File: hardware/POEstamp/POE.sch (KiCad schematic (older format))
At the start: 56 parts, among them J1 0813-1X1T-57-F, P1 PoE-, P2 PoE+, P3 GND, P4 +5V, Q1 SI3440DV, NFET, Q2 MMBTA42, Q3 2N7002, T1 PA1134, U1 LTC4267-3, U3 PS2811

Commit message: Finished adding BOM info to schematic. Swapped around a couple more symbols and footprints. Ran DRC and corrected one error.
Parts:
- removed Q2: MMBTA42, SMD_Packages:SOT-23_Inv2, symbol NPN
- removed Q3: 2N7002, SMD_Packages:SOT-23-GDS, symbol MOSFET_N
- removed R21: 470R, IPC7351-Nominal:RESC1608X55, symbol R-RESCUE-POE
- added P5: CONN_01X05, symbol CONN_01X05
- added P6: 5Vout, symbol TST
- added P7: GNDout, symbol TST
- added Q2: 2N7002, smd-semi:SOT-23, symbol MMBF170
- added Q3: MMBTA42, smd-semi:SOT-23, symbol MMBT3904
- added R21: 470R, IPC7351-Nominal:RESC1608X55, symbol R
- J1: Vend1 (none) -> Digikey; Vend1Id (none) -> 507-1421-ND
- Q1: footprint (none) -> rfid:TSOP-6; Vend1 (none) -> Digikey; Vend1Id (none) -> SI3440DV-T1-E3CT-ND
- T1: Vend1 (none) -> Digikey; Vend1Id (none) -> 553-1982-1-ND
- U3: Vend1 (none) -> Digikey; Vend1Id (none) -> PS2811-1ACT-ND
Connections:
- net 5VPoE: now also P6.1, R21.1
- net GND: now also P7.1
- net GNDA: now also Q2.2 (S)
- net Ith/Run: now also Q2.3 (D)
- net PVcc: now also Q3.2 (E)
- net TPIN+: now also P5.3 (P3)
- net TPIN-: now also P5.4 (P4)
- net TPOUT+: now also P5.1 (P1)
- net TPOUT-: now also P5.2 (P2)
- net at C2.1, C3.1, L1.2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: now also Q3.3 (C)
- net at D5.2 (K), R2.2: now also Q3.1 (B)
- net at D4.2 (K), R1.2: now also Q2.1 (G)
- net at C12.1, C13.1, R11.1: now also R21.2
- net CT: now reaches J1.7 (CT)
- net CT: now also P5.5 (P5)
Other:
- note added: "Power out"
- note added: "power good\nvisual indicator"
- note removed: "power good visual indicator"
- moved on the sheet: D12, R22
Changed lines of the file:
@@
-$EndComp
-$Comp
-L NPN Q2
-U 1 1 52997F92
-P 7450 3205
-F 0 "Q2" H 7450 3055 50  0000 R CNN
-F 1 "MMBTA42" H 7450 3355 50  0000 R CNN
-F 2 "SMD_Packages:SOT-23_Inv2" H 7450 3205 60  0001 C CNN
-F 3 "" H 7450 3205 60  0000 C CNN
-	1    7450 3205
-	1    0    0    -1
 $EndComp
 $Comp
@@
 F 1 "PA1134" H 9815 3425 50  0000 C CNN
 F 2 "rfid:PA1134" V 9850 2865 60  0001 C CNN
-F 3 "" V 9850 2865 60  0000 C CNN
+F 3 "http://productfinder.pulseeng.com/products/datasheets/SPM2007_55.pdf" V 9850 2865 60  0001 C CNN
+F 4 "Digikey" H 9750 3015 60  0001 C CNN "Vend1"
+F 5 "553-1982-1-ND" H 9750 3015 60  0001 C CNN "Vend1Id"
 	1    9750 3015
 	1    0    0    -1
@@
 NoConn ~ 4450 4465
 $Comp
-L MOSFET_N Q3
-U 1 1 529FE736
-P 7300 4865
-F 0 "Q3" V 7150 5065 60  0000 R CNN
-F 1 "2N7002" V 7500 5015 60  0000 R CNN
-F 2 "SMD_Packages:SOT-23-GDS" H 7300 4865 60  0001 C CNN
-F 3 "" H 7300 4865 60  0000 C CNN
-	1    7300 4865
-	0    1    1    0
-$EndComp
-$Comp
 L DIODE-RESCUE-POE D7
 U 1 1 529FE790
@@
 F 1 "PS2811" H 10435 5940 70  0000 C CNN
 F 2 "rfid:SSOP-4" H 9995 5565 60  0001 C CNN
-F 3 "" H 9995 5565 60  0000 C CNN
+F 3 "http://www.cel.com/pdf/datasheets/ps2811.pdf" H 9995 5565 60  0001 C CNN
+F 4 "Digikey" H 9395 5565 60  0001 C CNN "Vend1"
+F 5 "PS2811-1ACT-ND" H 9395 5565 60  0001 C CNN "Vend1Id"
 	1    9395 5565
 	1    0    0    -1
@@
 $EndComp
 $Comp
-L R-RESCUE-POE R21
-U 1 1 52A00D3B
-P 11920 4315
-F 0 "R21" V 12000 4315 40  0000 C CNN
-F 1 "470R" V 11927 4316 40  0000 C CNN
-F 2 "IPC7351-Nominal:RESC1608X55" V 11850 4315 30  0001 C CNN
-F 3 "http://industrial.panasonic.com/www-cgi/jvcr13pz.cgi?E+PZ+3+AOA0002+ERJ3EKF4700V+7+WW" H 11920 4315 30  0001 C CNN
-F 4 "Digikey" V 11920 4315 60  0001 C CNN "Vend1"
-F 5 "P470HCT-ND" V 11920 4315 60  0001 C CNN "Vend1Id"
-	1    11920 4315
-	0    -1   -1   0
-$EndComp
-$Comp
 L R-RESCUE-POE R11
 U 1 1 52A00D4F
@@
 L LED-RESCUE-POE D12
 U 1 1 52A27A6E
-P 14475 3560
-F 0 "D12" H 14475 3660 50  0000 C CNN
-F 1 "5V LED" H 14480 3445 50  0000 C CNN
-F 2 "LEDs:LED-0603" H 14475 3560 60  0001 C CNN
-F 3 "http://www.osram-os.com/Graphics/XPic9/00128783_0.pdf" H 14475 3560 60  0001 C CNN
-F 4 "Digikey" H 14475 3560 60  0001 C CNN "Vend1"
-F 5 "475-1409-1-ND" H 14475 3560 60  0001 C CNN "Vend1Id"
-	1    14475 3560
+P 15270 3555
+F 0 "D12" H 15270 3655 50  0000 C CNN
+F 1 "5V LED" H 15275 3440 50  0000 C CNN
+F 2 "LEDs:LED-0603" H 15270 3555 60  0001 C CNN
+F 3 "http://www.osram-os.com/Graphics/XPic9/00128783_0.pdf" H 15270 3555 60  0001 C CNN
+F 4 "Digikey" H 15270 3555 60  0001 C CNN "Vend1"
+F 5 "475-1409-1-ND" H 15270 3555 60  0001 C CNN "Vend1Id"
+	1    15270 3555
 	0    1    1    0
 $EndComp
@@
 L GND-RESCUE-POE #PWR013
 U 1 1 52A27D1F
-P 14475 3825
-F 0 "#PWR013" H 14475 3825 30  0001 C CNN
-F 1 "GND" H 14475 3755 30  0001 C CNN
-F 2 "" H 14475 3825 60  0000 C CNN
-F 3 "" H 14475 3825 60  0000 C CNN
-	1    14475 3825
+P 15270 3820
+F 0 "#PWR013" H 15270 3820 30  0001 C CNN
+F 1 "GND" H 15270 3750 30  0001 C CNN
+F 2 "" H 15270 3820 60  0000 C CNN
+F 3 "" H 15270 3820 60  0000 C CNN
+	1    15270 3820
 	1    0    0    -1
 $EndComp
@@
 F 1 "0813-1X1T-57-F" H 1000 2200 60  0000 R CNN
 F 2 "rfid:0813-1X1T-57-F" H 1105 1730 60  0001 C CNN
-F 3 "" H 1105 1730 60  0000 C CNN
+F 3 "http://belfuse.com/pdfs/0813-1X1T-57-F.pdf" H 1105 1730 60  0001 C CNN
+F 4 "Digikey" H 1050 1600 60  0001 C CNN "Vend1"
+F 5 "507-1421-ND" H 1050 1600 60  0001 C CNN "Vend1Id"
 	1    1050 1600
 	-1   0    0    -1
@@
 L R-RESCUE-POE R22
 U 1 1 539D2B17
-P 14475 3040
-F 0 "R22" V 14555 3040 40  0000 C CNN
-F 1 "2.8k" V 14482 3041 40  0000 C CNN
-F 2 "IPC7351-Nominal:RESC1608X55" V 14405 3040 30  0001 C CNN
-F 3 "http://www.yageo.com/NewPortal/yageodocoutput?fileName=/pdf/R-Chip/PYu-RC_Group_51_RoHS_L_3.pdf" H 14475 3040 30  0001 C CNN
-F 4 "Digikey" V 14475 3040 60  0001 C CNN "Vend1"
-F 5 "311-2.80KHRCT-ND" V 14475 3040 60  0001 C CNN "Vend1Id"
-	1    14475 3040
+P 15270 3035
+F 0 "R22" V 15350 3035 40  0000 C CNN
+F 1 "2.8k" V 15277 3036 40  0000 C CNN
+F 2 "IPC7351-Nominal:RESC1608X55" V 15200 3035 30  0001 C CNN
+F 3 "http://www.yageo.com/NewPortal/yageodocoutput?fileName=/pdf/R-Chip/PYu-RC_Group_51_RoHS_L_3.pdf" H 15270 3035 30  0001 C CNN
+F 4 "Digikey" V 15270 3035 60  0001 C CNN "Vend1"
+F 5 "311-2.80KHRCT-ND" V 15270 3035 60  0001 C CNN "Vend1Id"
+	1    15270 3035
 	1    0    0    -1
 $EndComp
@@
 F 0 "Q1" H 9310 3765 60  0000 R CNN
 F 1 "SI3440DV, NFET" V 9595 4130 60  0000 R CNN
-F 2 "" H 9385 3625 60  0000 C CNN
-F 3 "" H 9385 3625 60  0000 C CNN
+F 2 "rfid:TSOP-6" H 9385 3625 60  0001 C CNN
+F 3 "http://www.vishay.com/docs/72380/72380.pdf" H 9385 3625 60  0001 C CNN
+F 4 "Digikey" H 9385 3625 60  0001 C CNN "Vend1"
+F 5 "SI3440DV-T1-E3CT-ND" H 9385 3625 60  0001 C CNN "Vend1Id"
 	1    9385 3625
 	1    0    0    -1
@@
 Text GLabel 12390 4210 1    60   Input ~ 0
 5VPoE
-Text GLabel 14475 2660 1    60   Input ~ 0
+Text GLabel 15270 2655 1    60   Input ~ 0
 5VPoE
-Text Notes 13860 2245 0    60   ~ 0
-power good visual indicator
+Text Notes 15035 2230 0    60   ~ 0
+power good\nvisual indicator
 $Comp
 L GNDA-RESCUE-POE #PWR016
@@
 	4200 4365 4450 4365
 Wire Wire Line
-	7900 3165 7900 3435
+	7900 3435 7900 3165
 Wire Wire Line
 	8450 3365 8600 3365
@@
 	4010 4065 4450 4065
 Wire Wire Line
-	7300 4565 7300 4665
-Wire Wire Line
-	6500 4565 7300 4565
+	6500 4565 7250 4565
 Wire Wire Line
 	6750 4965 7100 4965
@@
 Wire Wire Line
 	11505 2785 11620 2785
-Wire Wire Line
-	12390 4210 12390 4610
 Connection ~ 11620 2555
 Connection ~ 12595 2555
@@
 Connection ~ 12390 5225
 Wire Wire Line
-	11125 4315 11670 4315
+	11125 4315 11770 4315
 Wire Wire Line
 	10545 5365 11115 5365
-Wire Wire Line
-	12170 4315 12390 4315
-Connection ~ 12390 4310
 Connection ~ 2100 3915
 Wire Wire Line
@@
 Connection ~ 1485 4205
 Wire Wire Line
-	14475 2660 14475 2790
-Wire Wire Line
-	14475 3760 14475 3825
-Wire Wire Line
-	14475 3360 14475 3290
+	15270 2655 15270 2785
+Wire Wire Line
+	15270 3755 15270 3820
+Wire Wire Line
+	15270 3355 15270 3285
 Wire Wire Line
 	2060 1780 2150 1780
@@
 	1790 4510 1790 4580
 Wire Wire Line
-	2060 1100 2455 1100
+	2060 1100 2790 1100
 Wire Wire Line
 	1380 2150 1380 2195
@@
 Connection ~ 11545 2555
 Wire Wire Line
-	2060 1300 2455 1300
+	2060 1300 2790 1300
 Wire Wire Line
 	3705 2785 3705 2665
@@
 	3705 3185 3705 3235
 Wire Wire Line
-	2060 1400 2815 1400
-Wire Wire Line
-	2060 1600 2815 1600
+	2060 1400 2790 1400
+Wire Wire Line
+	2060 1600 2790 1600
 Wire Wire Line
 	11620 2785 11620 2555
@@
 	7700 4965 7700 4805
 Wire Wire Line
-	7550 3405 7550 3435
+	7550 3435 7550 3405
 Wire Wire Line
 	7000 3435 8025 3435
@@
 Wire Wire Line
 	12390 5110 12390 5650
+$Comp
+L MMBT3904 Q3
+U 1 1 565513CC
+P 7450 3205
+F 0 "Q3" H 7310 3430 50  0000 L CNN
+F 1 "MMBTA42" H 7065 3340 50  0000 L CNN
+F 2 "smd-semi:SOT-23" H 7650 3130 50  0001 L CIN
+F 3 "http://www.diodes.com/_files/datasheets/ds30062.pdf" H 7450 3205 50  0001 L CNN
+F 4 "Digikey" H 7450 3205 60  0001 C CNN "Vend1"
+F 5 "MMBTA42-FDICT-ND" H 7450 3205 60  0001 C CNN "Vend1Id"
+	1    7450 3205
+	1    0    0    -1
+$EndComp
+$Comp
+L MMBF170 Q2
+U 1 1 5655384D
+P 7300 4865
+F 0 "Q2" V 7200 4940 50  0000 L CNN
+F 1 "2N7002" V 7525 4730 50  0000 L CNN
+F 2 "smd-semi:SOT-23" H 7500 4790 50  0001 L CIN
+F 3 "http://www.diodes.com/_files/datasheets/ds11303.pdf" H 7300 4865 50  0001 L CNN
+F 4 "Digikey" H 7300 4865 60  0001 C CNN "Vend1"
+F 5 "2N7002-FDICT-ND" H 7300 4865 60  0001 C CNN "Vend1Id"
+	1    7300 4865
+	0    1    1    0
+$EndComp
+Wire Wire Line
+	7250 4565 7250 4665
+$Comp
+L CONN_01X05 P5
+U 1 1 56556854
+P 3175 1360
+F 0 "P5" H 3175 1660 50  0000 C CNN
+F 1 "CONN_01X05" V 3275 1360 50  0000 C CNN
+F 2 "" H 3175 1360 60  0000 C CNN
+F 3 "" H 3175 1360 60  0000 C CNN
+	1    3175 1360
+	1    0    0    -1
+$EndComp
+Wire Wire Line
+	2790 1100 2790 1160
+Wire Wire Line
+	2790 1160 2975 1160
+Wire Wire Line
+	2790 1300 2790 1260
+Wire Wire Line
+	2790 1260 2975 1260
+Wire Wire Line
+	2790 1400 2790 1360
+Wire Wire Line
+	2790 1360 2975 1360
+Wire Wire Line
+	2790 1600 2790 1460
+Wire Wire Line
+	2790 1460 2975 1460
+Wire Wire Line
+	2060 1200 2270 1200
+Text Label 2270 1200 2    39   ~ 0
+CT
+Wire Wire Line
+	2975 1560 2865 1560
+Text Label 2865 1560 0    39   ~ 0
+CT
+$Comp
+L TST P6
+U 1 1 56558BD3
+P 14090 2765
+F 0 "P6" H 14090 3065 50  0000 C BNN
+F 1 "5Vout" H 14090 3015 50  0000 C CNN
+F 2 "" H 14090 2765 60  0000 C CNN
+F 3 "" H 14090 2765 60  0000 C CNN
+	1    14090 2765
+	1    0    0    -1
+$EndComp
+$Comp
+L TST P7
+U 1 1 56558D34
+P 14360 2770
+F 0 "P7" H 14360 3070 50  0000 C BNN
+F 1 "GNDout" H 14360 3020 50  0000 C CNN
+F 2 "" H 14360 2770 60  0000 C CNN
+F 3 "" H 14360 2770 60  0000 C CNN
+	1    14360 2770
+	1    0    0    -1
+$EndComp
+Text GLabel 13900 2765 1    39   Input ~ 0
+5VPoE
+$Comp
+L GND-RESCUE-POE #PWR019
+U 1 1 56559A10
+P 14360 2830
+F 0 "#PWR019" H 14360 2830 30  0001 C CNN
+F 1 "GND" H 14360 2760 30  0001 C CNN
+F 2 "" H 14360 2830 60  0000 C CNN
+F 3 "" H 14360 2830 60  0000 C CNN
+	1    14360 2830
+	1    0    0    -1
+$EndComp
+Wire Wire Line
+	14360 2770 14360 2830
+Wire Wire Line
+	14090 2765 14090 2830
+Wire Wire Line
+	14090 2830 13900 2830
+Wire Wire Line
+	13900 2830 13900 2765
+Text Notes 13965 2300 0    59   ~ 0
+Power out
+$Comp
+L R R21
+U 1 1 5655CABE
+P 11920 4315
+F 0 "R21" V 12000 4315 50  0000 C CNN
+F 1 "470R" V 11920 4315 50  0000 C CNN
+F 2 "IPC7351-Nominal:RESC1608X55" V 11850 4315 30  0001 C CNN
+F 3 "http://industrial.panasonic.com/www-cgi/jvcr13pz.cgi?E+PZ+3+AOA0002+ERJ3EKF4700V+7+WW" H 11920 4315 30  0001 C CNN
+F 4 "Digikey" V 11920 4315 60  0001 C CNN "Vend1"
+F 5 "P470HCT-ND" V 11920 4315 60  0001 C CNN "Vend1Id"
+	1    11920 4315
+	0    1    1    0
+$EndComp
+Wire Wire Line
+	12390 4210 12390 4610
+Wire Wire Line
+	12070 4315 12390 4315
+Connection ~ 12390 4315
 $EndSCHEMATC

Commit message: Added last couple of footprints for generic connection points.
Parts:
- P5: footprint (none) -> conn-2mm:CONN-2MM-F-1x5
- P6, P7: footprint (none) -> Connect:1pin
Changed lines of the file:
@@
 F 0 "P5" H 3175 1660 50  0000 C CNN
 F 1 "CONN_01X05" V 3275 1360 50  0000 C CNN
-F 2 "" H 3175 1360 60  0000 C CNN
+F 2 "conn-2mm:CONN-2MM-F-1x5" H 3175 1360 60  0001 C CNN
 F 3 "" H 3175 1360 60  0000 C CNN
 	1    3175 1360
@@
 F 0 "P6" H 14090 3065 50  0000 C BNN
 F 1 "5Vout" H 14090 3015 50  0000 C CNN
-F 2 "" H 14090 2765 60  0000 C CNN
+F 2 "Connect:1pin" H 14090 2765 60  0001 C CNN
 F 3 "" H 14090 2765 60  0000 C CNN
 	1    14090 2765
@@
 F 0 "P7" H 14360 3070 50  0000 C BNN
 F 1 "GNDout" H 14360 3020 50  0000 C CNN
-F 2 "" H 14360 2770 60  0000 C CNN
+F 2 "Connect:1pin" H 14360 2770 60  0001 C CNN
 F 3 "" H 14360 2770 60  0000 C CNN
 	1    14360 2770

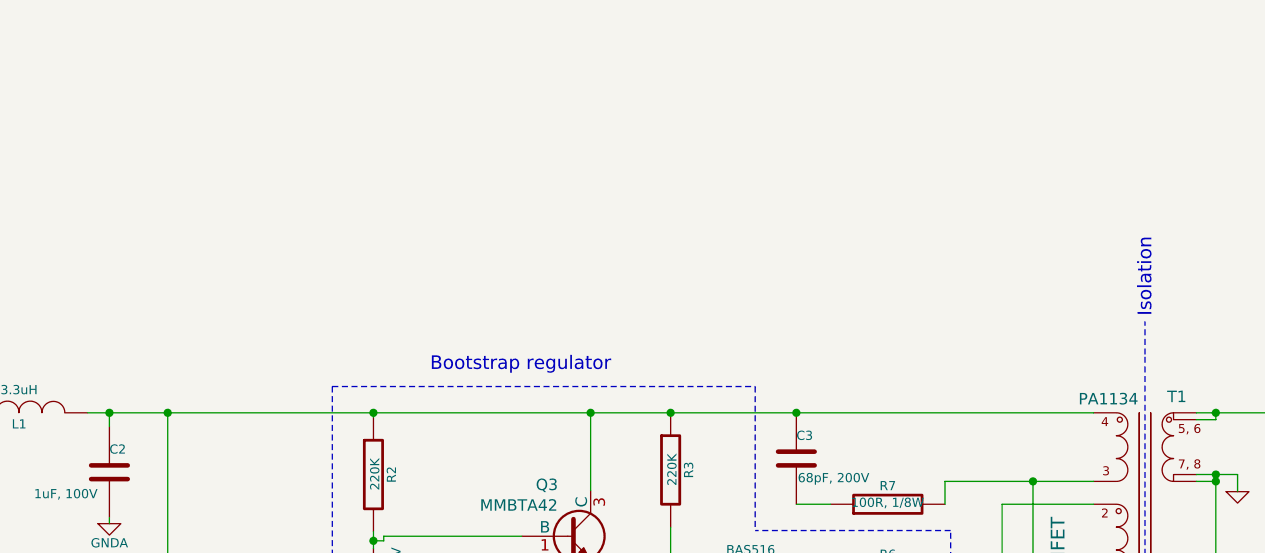
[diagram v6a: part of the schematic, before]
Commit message: Added note about replacing components in the non isolated side due to thermal issues.
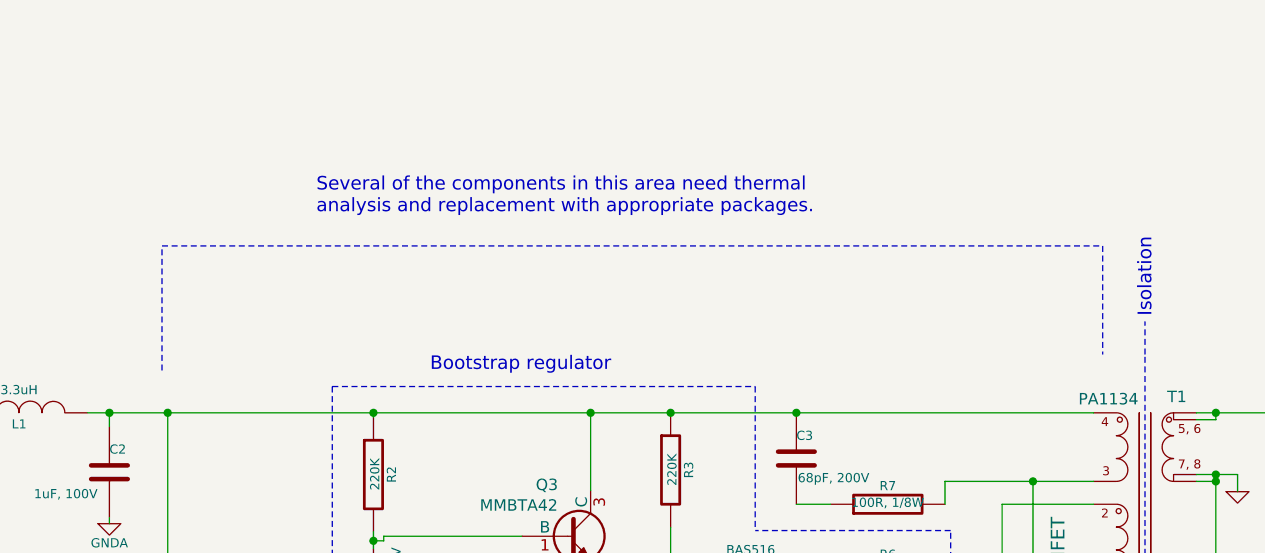
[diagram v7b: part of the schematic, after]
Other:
- note added: "Several of the components in this area need thermal \nanalysis and replacement with appropriate packages."
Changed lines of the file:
@@
 	12070 4315 12390 4315
 Connection ~ 12390 4315
+Wire Notes Line
+	5675 2480 5675 1935
+Wire Notes Line
+	5675 1935 9790 1935
+Wire Notes Line
+	9790 1935 9790 2410
+Text Notes 6350 1800 0    59   ~ 0
+Several of the components in this area need thermal \nanalysis and replacement with appropriate packages.
 $EndSCHEMATC

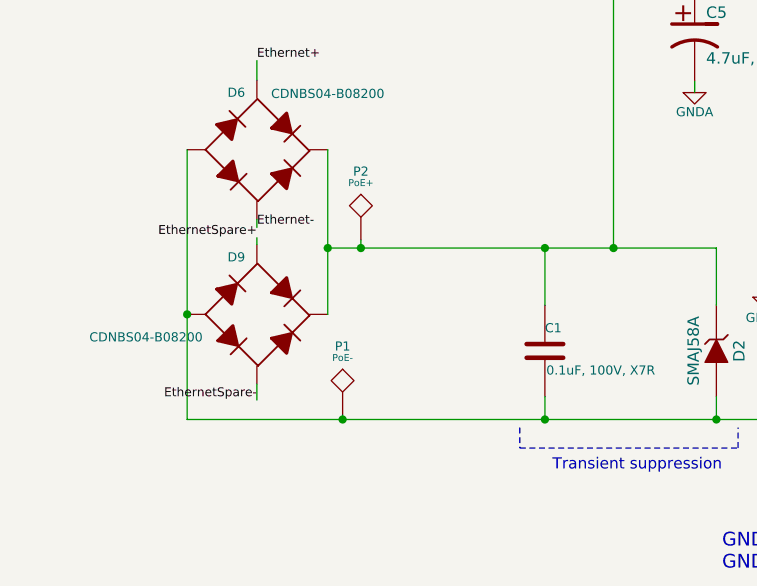
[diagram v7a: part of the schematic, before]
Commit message: Removed two unnecessary test points and changed footprints on two others to SMD pads.
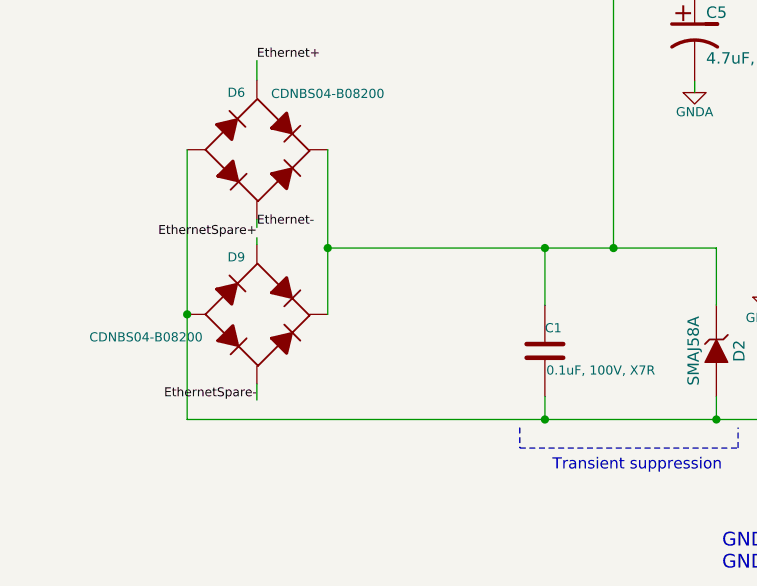
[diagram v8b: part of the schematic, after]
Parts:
- removed P1: PoE-, Connect:PINTST, symbol TST
- removed P2: PoE+, Connect:PINTST, symbol TST
- P3, P4: footprint Connect:PINTST -> Measurement_Points:Measurement_Point_Round-SMD-Pad_Big
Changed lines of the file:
@@
 F 0 "P4" H 11545 2820 40  0000 C CNN
 F 1 "+5V" H 11545 2770 30  0000 C CNN
-F 2 "Connect:PINTST" H 11545 2520 60  0001 C CNN
+F 2 "Measurement_Points:Measurement_Point_Round-SMD-Pad_Big" H 11545 2520 60  0001 C CNN
 F 3 "" H 11545 2520 60  0000 C CNN
 	1    11545 2520
@@
 F 0 "P3" H 11900 6435 40  0000 C CNN
 F 1 "GND" H 11900 6385 30  0000 C CNN
-F 2 "Connect:PINTST" H 11900 6135 60  0001 C CNN
+F 2 "Measurement_Points:Measurement_Point_Round-SMD-Pad_Big" H 11900 6135 60  0001 C CNN
 F 3 "" H 11900 6135 60  0000 C CNN
 	1    11900 6135
-	1    0    0    -1
-$EndComp
-$Comp
-L TST P2
-U 1 1 52A27A0E
-P 2245 3880
-F 0 "P2" H 2245 4180 40  0000 C CNN
-F 1 "PoE+" H 2245 4130 30  0000 C CNN
-F 2 "Connect:PINTST" H 2245 3880 60  0001 C CNN
-F 3 "" H 2245 3880 60  0000 C CNN
-	1    2245 3880
-	1    0    0    -1
-$EndComp
-$Comp
-L TST P1
-U 1 1 52A27A22
-P 2165 4645
-F 0 "P1" H 2165 4945 40  0000 C CNN
-F 1 "PoE-" H 2165 4895 30  0000 C CNN
-F 2 "Connect:PINTST" H 2165 4645 60  0001 C CNN
-F 3 "" H 2165 4645 60  0000 C CNN
-	1    2165 4645
 	1    0    0    -1
 $EndComp
@@
 	1380 2150 1380 2195
 Wire Wire Line
-	2165 4645 2165 4665
-Connection ~ 2165 4665
-Wire Wire Line
-	2245 3915 2245 3880
-Connection ~ 2245 3915
-Wire Wire Line
 	11900 6165 11900 6135
